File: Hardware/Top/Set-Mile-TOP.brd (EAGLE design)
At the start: 38 x 38 mm, 19 parts, among them U2 NRF52832_MODULE_MDBT42

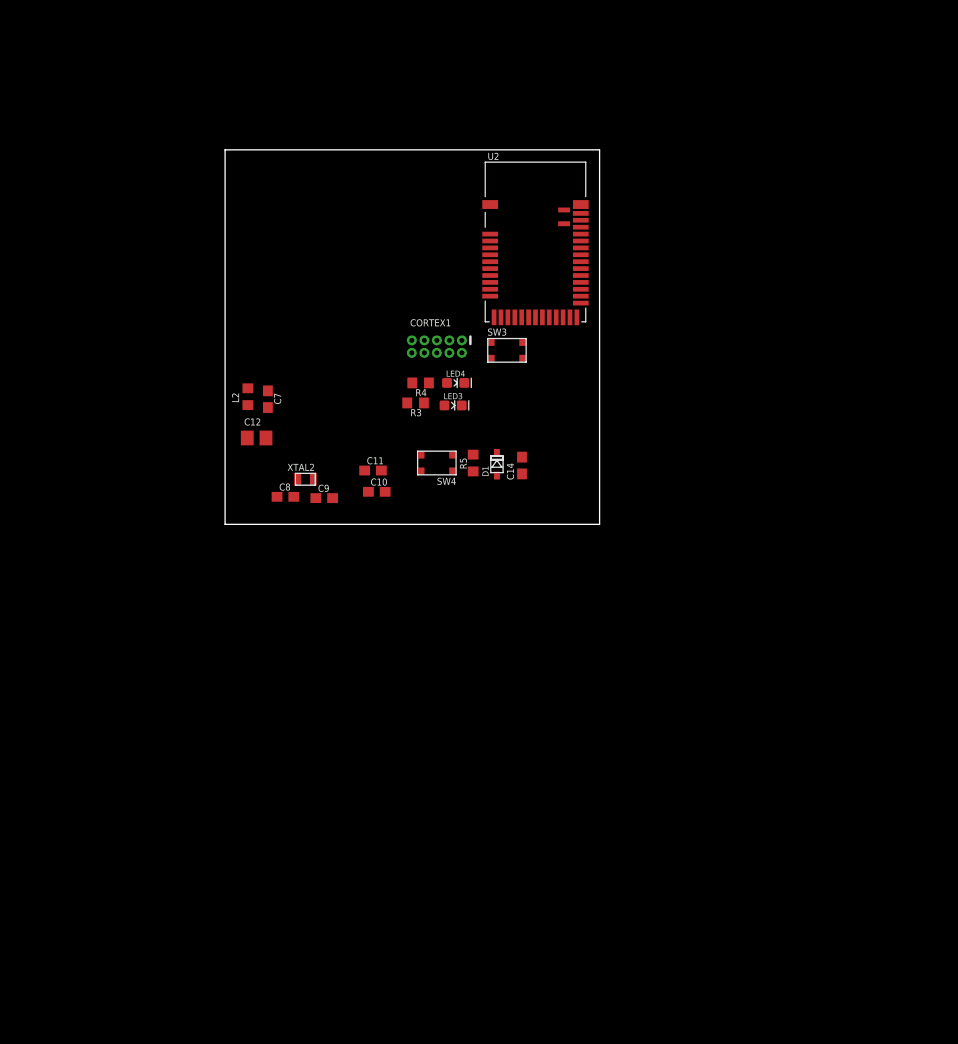
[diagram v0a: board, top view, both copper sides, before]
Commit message: Top Board Electronics Placed
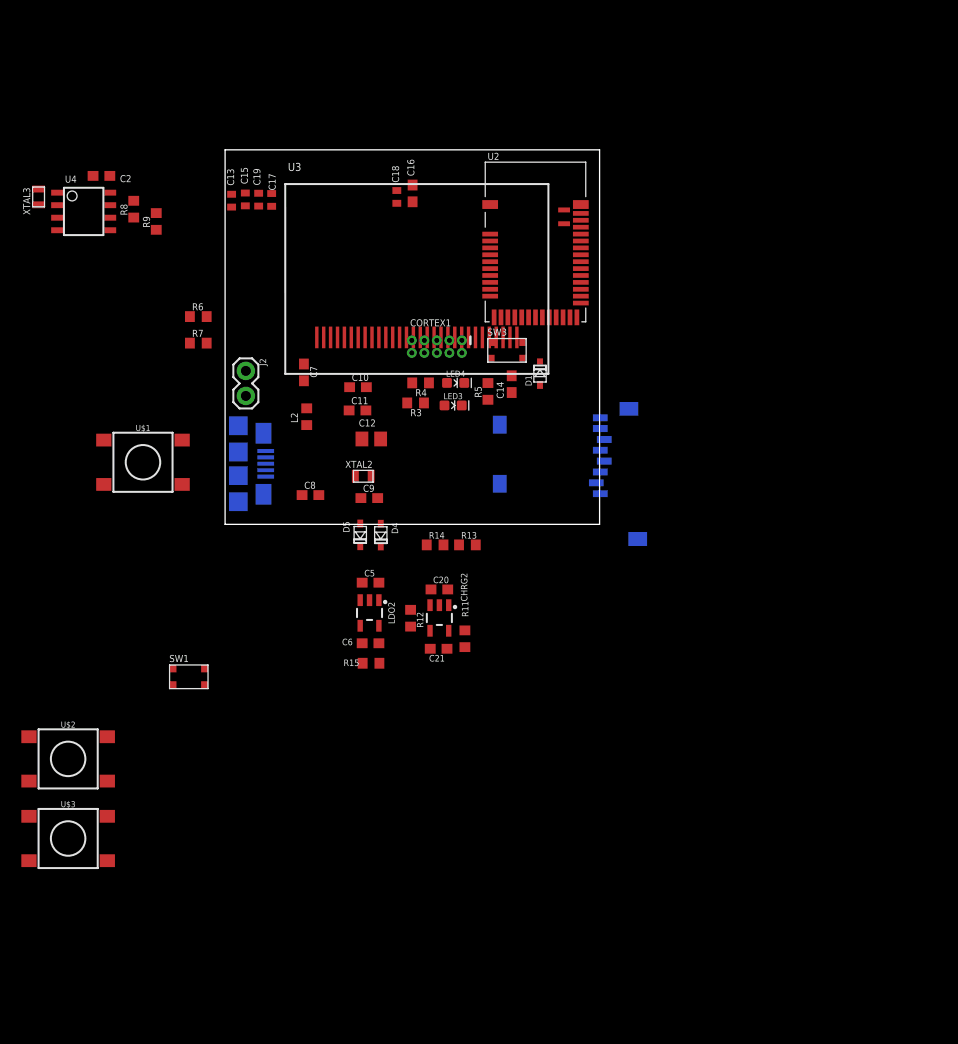
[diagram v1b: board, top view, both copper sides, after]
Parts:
- removed SW4: (no value), LinnesLab-Switches:BUTTON-GULLWING
- added C13, C15, C17, C18, C19: 2.2uF, LinnesLab-Passives:C0402
- added C16: 10uF, LinnesLab-Passives:C0603
- added C2, C5, C6: 1u, LinnesLab-Passives:C0603
- added C20, C21: 4.7u, LinnesLab-Passives:C0603
- added CHRG2: MCP73831, LinnesLab-Power:SOT23-5
- added D4, D5: (no value), LinnesLab-DiscreteSemi:USC
- added J2: (no value), LinnesLab-Connectors:1X02
- added LDO2: MIC5504, LinnesLab-Power:SOT23-5
- added R11: (no value), LinnesLab-Passives:R0603
- added R12, R13, R14, R15: 100k, LinnesLab-Passives:R0603
- added R6, R8, R9: 10k, LinnesLab-Passives:R0603
- added R7: 390k, LinnesLab-Passives:R0603
- added SD2: (no value), LinnesLab-Connectors:MICROSD
- added SW1: (no value), LinnesLab-Switches:BUTTON-GULLWING
- added U$1, U$2, U$3: SWITCH.MOM, LinnesLab-Switches:TACTILE_SWITCH_SMD_6.2MM_TALL
- added U3: (no value), LinnesLab-Displays:UG-2864HSWEG01_0.96IN_NO-WRAPAROUND
- added U4: PCF8523, LinnesLab-Clocks:SO8
- added USB2: USB.MICRO-BIGGERPADS, LinnesLab-Connectors:USB-MICRO-01.BIGGERPADS
- added XTAL3: 32.7680kHz, LinnesLab-Clocks:2-SMD.NOLEAD.2.0MMTO1.2MM
- moved C12 11.6 mm to (14.8, 8.66)
- moved C10 10.8 mm to (13.5, 13.9)
- moved D1 10.2 mm to (32.0, 15.3)
- moved C14 8.32 mm to (29.1, 14.2)
- moved R5 7.42 mm to (26.7, 13.5)
- moved L2 6.31 mm to (8.28, 10.9)
- moved C11 6.30 mm to (13.4, 11.6)
- moved XTAL2 5.88 mm to (14.0, 4.88)
- moved C9 4.57 mm to (14.6, 2.67)
- moved C7 4.56 mm to (8.00, 15.4)
- moved C8 2.55 mm to (8.66, 2.97)
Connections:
- new net BATT: R13.1, R14.2
- new net CD1: SD2.CD1
- new net CD2: SD2.CD2
- new net CHRG.STAT: CHRG2.1, R12.1
- new net CS.OLED: U3.13
- new net DC.OLED: U3.15
- new net N$1: R6.2, U3.11
- new net N$13: C16.2, U3.28
- new net N$15: C18.2, U3.27
- new net N$17: CHRG2.5, R11.2
- new net N$19: U4.2, XTAL3.P$1
- new net N$2: R7.1, U3.26
- new net N$20: U4.1, XTAL3.P$2
- new net N$3: C13.2, U3.2
- new net N$5: C13.1, U3.3
- new net N$7: C15.2, U3.4
- new net N$8: C15.1, U3.5
- new net RESET.OLED: U3.14
- new net SD.CS: SD2.2
- new net SW1: U$1.A1, U$2.A1, U$3.A1
- new net USB+: USB2.3
- new net USB-: USB2.2
- new net VBATT: U4.3
- new net VIN: C21.2, C5.2, CHRG2.4, D4.-, D5.-, LDO2.1, LDO2.3, R12.2
- new net VLIPO: C20.1, CHRG2.3, D4.+, J2.2, R13.2
- new net V_USB: D5.+, USB2.1
- net 3.3V: now also C17.2, C19.2, C2.1, C6.1, LDO2.5, R15.2, R8.2, R9.2, SD2.4, U3.6, U3.9, U4.8
- net DFU: now also SW1.3
- net GND: now also C16.1, C17.1, C18.1, C19.1, C2.2, C20.2, C21.1, C5.1, C6.2, CHRG2.2, J2.1, LDO2.2, R11.1, R14.1, R15.1, R6.1, R7.2, SD2.6, SD2.MT1, SD2.MT2, SW1.1, U$1.B1, U$1.B2, U$2.B1, U$2.B2, U$3.B1, U$3.B2, U3.1, U3.10, U3.12, U3.29, U3.30, U3.8, U4.4, USB2.5, USB2.S1, USB2.S2, USB2.S3, USB2.S4, USB2.S5, USB2.S6; no longer SW4.3
- net MISO: now also SD2.7
- net MOSI: now also SD2.3, U3.19
- net RESET: no longer SW4.1
- net SCK: now also SD2.5, U3.18
- net SCL: now also R8.1, U4.6
- net SDA: now also R9.1, U4.5

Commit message: updated board design to section 2
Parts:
- removed U$1, U$2, U$3: SWITCH.MOM, LinnesLab-Switches:TACTILE_SWITCH_SMD_6.2MM_TALL
- added C22: 100n, LinnesLab-Passives:C0603
- added C23, C24: 47p, LinnesLab-Passives:C0603
- added J1: (no value), LinnesLab-Connectors:1X07
- added JP2: (no value), LinnesLab-Switches:SMT-JUMPER_2_NO_SILK
- added LED5: RED, LinnesLab-LED:LED-0603
- added LED6: YELLOW, LinnesLab-LED:LED-0603
- added R1, R2: 0, LinnesLab-Passives:R0603
- added R17, R18: 27, LinnesLab-Passives:R0603
- added R19, R20: 1k, LinnesLab-Passives:R0603
- added SWITCH1, SWITCH2: SWITCH.MOM, LinnesLab-Switches:TACTILE_SWITCH_SMD_6.2MM_TALL
- added U5: FT231XS, LinnesLab-DigitalIC:SSOP20_L
- moved R9 81.8 mm to (-19.3, -50.2), turned to 0 degrees
- moved R8 79.3 mm to (-19.3, -46.7), turned to 0 degrees
- moved CORTEX1 33.8 mm to (55.1, 14.3)
- moved C15 10.4 mm to (9.40, 25.6)
- moved C13 10.4 mm to (8.15, 25.6)
- moved C19 10.3 mm to (10.6, 25.6)
- moved C17 10.2 mm to (11.8, 25.6)
- moved U2 0.42 mm to (31.4, 29.1)
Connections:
- net VBATT renamed VBAT
- removed net BATT: R13.1, R14.2
- removed net CD1: SD2.CD1
- removed net CHRG.STAT: CHRG2.1, R12.1
- removed net CS.OLED: U3.13
- removed net DC.OLED: U3.15
- removed net RESET.OLED: U3.14
- removed net RXD: U2.21
- removed net SD.CS: SD2.2
- removed net SW1: U$1.A1, U$2.A1, U$3.A1
- removed net TXD: U2.19
- new net !CTS: JP2.2, U5.9
- new net !DTR: U5.1
- new net A4/BATT: R13.1, R14.2, U2.5
- new net A6/TIA: J1.5, U2.7
- new net A7/PPG: J1.7, U2.8
- new net D11/SW1: SWITCH1.A1, U2.25
- new net D15/SW2: SWITCH2.A1, U2.29
- new net D16/CS.OLED: U2.30, U3.13
- new net D27/CHRG.STATUS: CHRG2.1, R12.1, U2.4
- new net D29/LED.CTRL: J1.6
- new net D3/RESET.OLED: U2.16, U3.14
- new net D4/DC.OLED: U2.15, U2.17, U3.15
- new net D5/CD1: SD2.CD1, U2.18
- new net D7/SD.CS: SD2.2, U2.20
- new net D9/LED.CTRL: U2.6
- new net FT3V3: U5.13
- new net N$23: R17.2, U5.12
- new net N$24: R18.2, U5.11
- new net N$25: LED5.C, R19.2
- new net N$26: LED6.C, R20.2
- new net RXD.FT: R2.1, U5.4
- new net RXD.NRF: R1.2, U2.21
- new net RXLED: R19.1, U5.17
- new net TXD.FT: R1.1, U5.20
- new net TXD.NRF: R2.2, U2.19
- new net TXLED: R20.1, U5.10
- net 3.3V: now also C22.2, LED5.A, LED6.A, U5.14, U5.3
- net GND: now also C22.1, C23.2, C24.1, JP2.1, SWITCH1.B1, SWITCH1.B2, SWITCH2.B1, SWITCH2.B2, U5.16, U5.6; no longer U$1.B1, U$1.B2, U$2.B1, U$2.B2, U$3.B1, U$3.B2
- net SCL: now also R9.1; no longer R8.1
- net SDA: now also R8.1; no longer R9.1
- net USB+: now also C23.1, R18.1
- net USB-: now also C24.2, R17.1
- net V_USB: now also U5.15

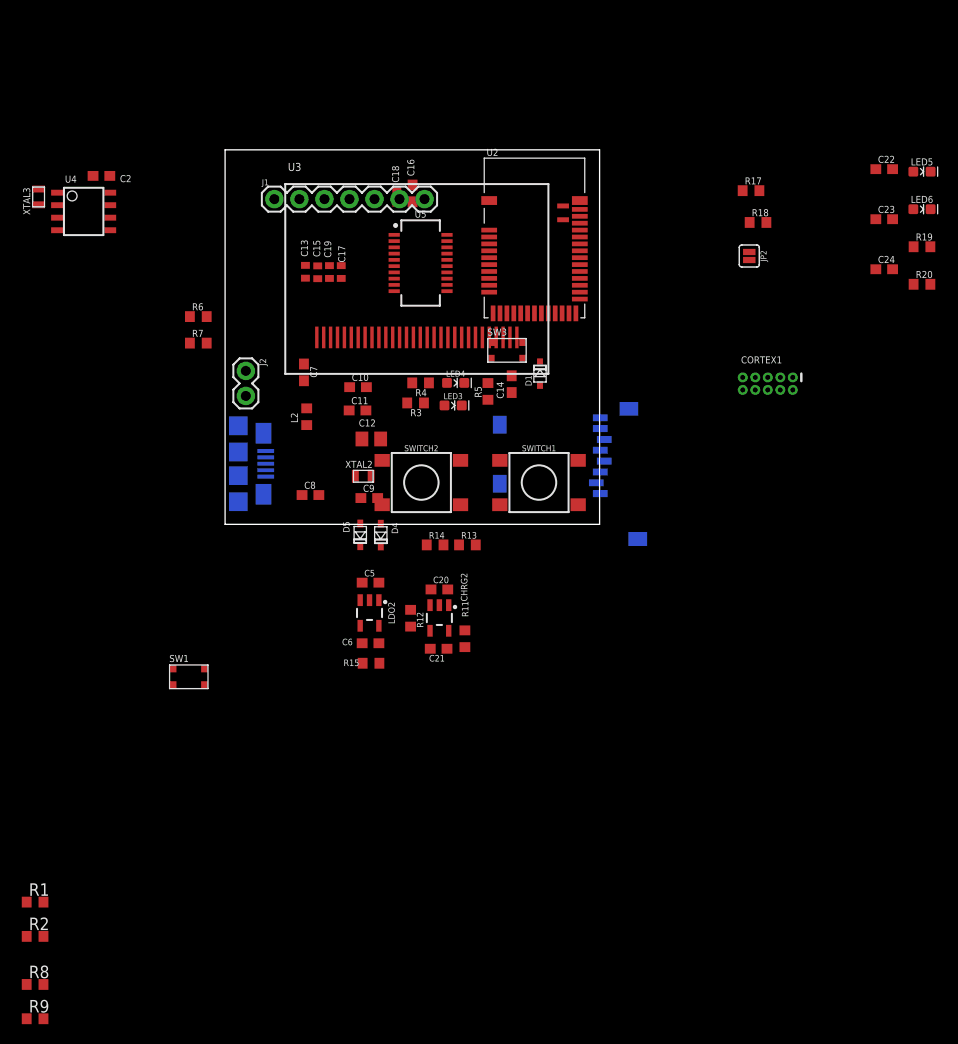
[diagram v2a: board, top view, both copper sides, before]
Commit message: routing bottom board and oranized top board
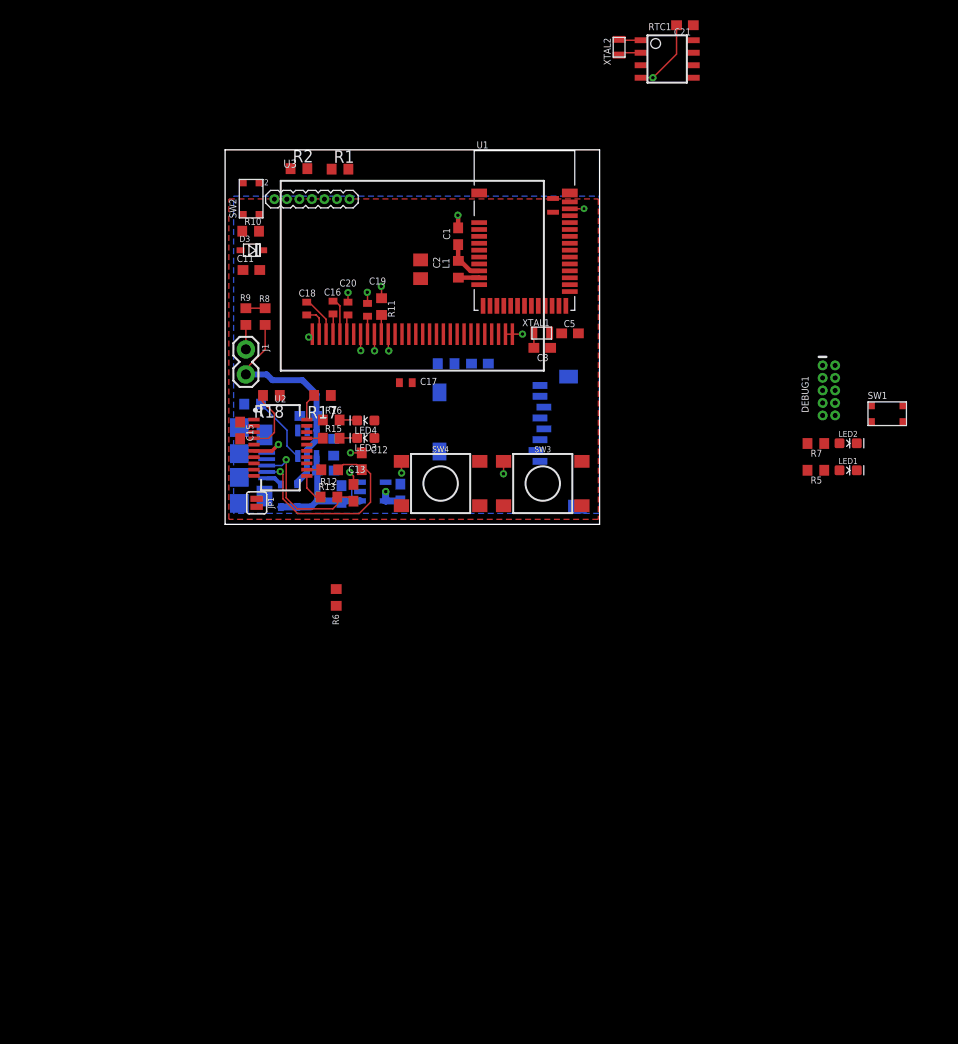
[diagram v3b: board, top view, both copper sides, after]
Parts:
- removed C22: 100n, LinnesLab-Passives:C0603
- removed C23, C24: 47p, LinnesLab-Passives:C0603
- removed C7: 1u, LinnesLab-Passives:C0603
- removed C8: (no value), LinnesLab-Passives:C0603
- removed CHRG2: MCP73831, LinnesLab-Power:SOT23-5
- removed CORTEX1: CORTEX_DEBUG_PTH, LinnesLab-Connectors:2X5-PTH-1.27MM
- removed D4, D5: (no value), LinnesLab-DiscreteSemi:USC
- removed JP2: (no value), LinnesLab-Switches:SMT-JUMPER_2_NO_SILK
- removed L2: 10u, LinnesLab-Passives:L0603
- removed LDO2: MIC5504, LinnesLab-Power:SOT23-5
- removed LED5: RED, LinnesLab-LED:LED-0603
- removed LED6: YELLOW, LinnesLab-LED:LED-0603
- removed R19, R20: 1k, LinnesLab-Passives:R0603
- removed SD2: (no value), LinnesLab-Connectors:MICROSD
- removed SWITCH1, SWITCH2: SWITCH.MOM, LinnesLab-Switches:TACTILE_SWITCH_SMD_6.2MM_TALL
- removed U4: PCF8523, LinnesLab-Clocks:SO8
- removed U5: FT231XS, LinnesLab-DigitalIC:SSOP20_L
- removed USB2: USB.MICRO-BIGGERPADS, LinnesLab-Connectors:USB-MICRO-01.BIGGERPADS
- removed XTAL3: 32.7680kHz, LinnesLab-Clocks:2-SMD.NOLEAD.2.0MMTO1.2MM
- added C1: 1u, LinnesLab-Passives:C0603
- added C3: (no value), LinnesLab-Passives:C0603
- added C4: 4.7u, LinnesLab-Passives:C0603
- added CHRG1: MCP73831, LinnesLab-Power:SOT23-5
- added D2, D3: (no value), LinnesLab-DiscreteSemi:USC
- added DEBUG1: CORTEX_DEBUG_PTH, LinnesLab-Connectors:2X5-PTH-1.27MM
- added JP1: (no value), LinnesLab-Switches:SMT-JUMPER_2_NO_SILK
- added L1: 10u, LinnesLab-Passives:L0603
- added LDO1: MIC5504, LinnesLab-Power:SOT23-5
- added LED1: RED, LinnesLab-LED:LED-0603
- added LED2: BLUE, LinnesLab-LED:LED-0603
- added R10: 10k, LinnesLab-Passives:R0603
- added R16: 1k, LinnesLab-Passives:R0603
- added RTC1: PCF8523, LinnesLab-Clocks:SO8
- added SD1: (no value), LinnesLab-Connectors:MICROSD
- added SW2: (no value), LinnesLab-Switches:BUTTON-GULLWING
- added SW4: SWITCH.MOM, LinnesLab-Switches:TACTILE_SWITCH_SMD_6.2MM_TALL
- added U1: NRF52832_MODULE_MDBT42, LinnesLab-Microcontrollers:BLE_MODULE_RAYTAC_MDBT42
- added USB1: USB.MICRO-BIGGERPADS, LinnesLab-Connectors:USB-MICRO-01.BIGGERPADS
- added XTAL1: 32.768kHz, LinnesLab-Clocks:2-SMD.NOLEAD.2.0MMTO1.2MM
- C10: value 300p -> 4.7u
- C11: value 300p -> 100n
- C12: value 10u -> 47p; device LinnesLab-Passives:C0805 -> LinnesLab-Passives:C0603
- C13: value 2.2uF -> 47p; device LinnesLab-Passives:C0402 -> LinnesLab-Passives:C0603
- C14: value 100n -> 10uF
- C15: value 2.2uF -> 100n; device LinnesLab-Passives:C0402 -> LinnesLab-Passives:C0603
- C16: value 10uF -> 2.2uF; device LinnesLab-Passives:C0603 -> LinnesLab-Passives:C0402
- C2: value 1u -> 10u; device LinnesLab-Passives:C0603 -> LinnesLab-Passives:C0805
- C20: value 4.7u -> 2.2uF; device LinnesLab-Passives:C0603 -> LinnesLab-Passives:C0402
- C21: value 4.7u -> 1u
- C5: value 1u -> (none)
- C9: value (none) -> 1u
- J1: device LinnesLab-Connectors:1X07 -> LinnesLab-Connectors:1X02
- J2: device LinnesLab-Connectors:1X02 -> LinnesLab-Connectors:1X07_1.27MM
- LED4: value BLUE -> YELLOW
- R1, R2: value 0 -> 10k
- R11: value (none) -> 10k
- R12, R13: value 100k -> 27
- R14: value 100k -> 390k
- R15: value 100k -> 1k
- R17, R18: value 27 -> 0
- R3: value 1k -> 100k
- R4: value 1k -> (none)
- R5: value 10k -> 1k
- R6, R8, R9: value 10k -> 100k
- R7: value 390k -> 1k
- SW3: value (none) -> SWITCH.MOM; device LinnesLab-Switches:BUTTON-GULLWING -> LinnesLab-Switches:TACTILE_SWITCH_SMD_6.2MM_TALL
- U2: value NRF52832_MODULE_MDBT42 -> FT231XS; device LinnesLab-Microcontrollers:BLE_MODULE_RAYTAC_MDBT42 -> LinnesLab-DigitalIC:SSOP20_L
- XTAL2: value 32.768kHz -> 32.7680kHz
- moved R2 82.4 mm to (7.49, 36.1)
- moved R1 80.5 mm to (11.7, 36.0)
- moved SW1 75.7 mm to (67.2, 11.2)
- moved R9 74.4 mm to (2.11, 21.1), turned to 90 degrees
- moved R8 71.7 mm to (4.06, 21.1), turned to 270 degrees
- moved C21 68.0 mm to (46.7, 50.6)
- moved R7 63.5 mm to (59.9, 8.20), turned to 180 degrees
- moved R18 52.4 mm to (4.70, 13.1)
- moved XTAL2 50.7 mm to (40.0, 48.4), turned to 90 degrees
- moved R17 48.2 mm to (9.88, 13.1)
- moved R11 34.8 mm to (15.9, 22.1), turned to 270 degrees
- moved R5 34.2 mm to (59.9, 5.49), turned to 180 degrees
- moved C2 33.7 mm to (19.8, 25.9), turned to 270 degrees
- moved U2 33.4 mm to (5.61, 7.77), turned to 270 degrees
- moved C5 32.4 mm to (35.0, 19.4)
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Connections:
- removed net VBAT: U4.3
- net !CTS: now also JP1.2, U2.9; no longer JP2.2, U5.9
- net !DTR: now also U2.1; no longer U5.1
- net 3.3V: now also C15.2, C2.2, C20.2, C21.1, C9.1, D3.-, DEBUG1.1, J2.4, LDO1.5, LED3.A, LED4.A, R1.2, R10.2, R2.2, R6.2, RTC1.8, SD1.4, U1.11, U2.14, U2.3; no longer C12.2, C17.2, C2.1, C22.2, C6.1, CORTEX1.1, D1.-, LDO2.5, LED5.A, LED6.A, R15.2, R5.2, R8.2, R9.2, SD2.4, U2.11, U4.8, U5.14, U5.3
- net A4/BATT: now also R8.1, R9.2, U1.5; no longer R13.1, R14.2, U2.5
- net A6/TIA: now also J2.6, U1.7; no longer J1.5, U2.7
- net A7/PPG: now also J2.7, U1.8; no longer J1.7, U2.8
- net CD2: now also SD1.CD2; no longer SD2.CD2
- net D11/SW1: now also SW3.A1, U1.25; no longer SWITCH1.A1, U2.25
- net D15/SW2: now also SW4.A1, U1.29; no longer SWITCH2.A1, U2.29
- net D16/CS.OLED: now also U1.30; no longer U2.30
- net D27/CHRG.STATUS: now also CHRG1.1, R3.1, U1.4; no longer CHRG2.1, R12.1, U2.4
- net D29/LED.CTRL: now also J2.5; no longer J1.6
- net D3/RESET.OLED: now also U1.16; no longer U2.16
- net D4/DC.OLED: now also U1.15, U1.17; no longer U2.15, U2.17
- net D5/CD1: now also SD1.CD1, U1.18; no longer SD2.CD1, U2.18
- net D7/SD.CS: now also SD1.2, U1.20; no longer SD2.2, U2.20
- net D9/LED.CTRL: now also U1.6; no longer U2.6
- net DFU: now also SW2.3, U1.34; no longer SW3.3, U2.34
- net DTR: now also C11.1; no longer C14.1
- net FRST: now also U1.38; no longer U2.38
- net FT3V3: now also U2.13; no longer U5.13
- net GND: now also C1.2, C13.2, C14.1, C15.1, C2.1, C20.1, C21.2, C3.1, C4.1, C5.2, C6.1, CHRG1.2, DEBUG1.3, DEBUG1.5, DEBUG1.7, DEBUG1.9, J1.1, J2.3, JP1.1, LDO1.2, LED1.C, LED2.C, R14.2, R4.1, R9.1, RTC1.4, SD1.6, SD1.MT1, SD1.MT2, SW2.1, SW3.B1, SW3.B2, SW4.B1, SW4.B2, U1.1, U1.12, U1.24, U1.39, U2.16, U2.6, USB1.5, USB1.S1, USB1.S2, USB1.S3, USB1.S4, USB1.S5, USB1.S6; no longer C11.2, C16.1, C18.1, C2.2, C20.2, C21.1, C22.1, C23.2, C24.1, C5.1, C6.2, C7.2, C8.1, CHRG2.2, CORTEX1.3, CORTEX1.5, CORTEX1.7, CORTEX1.9, J2.1, JP2.1, LDO2.2, LED3.C, LED4.C, R14.1, R15.1, R7.2, SD2.6, SD2.MT1, SD2.MT2, SW3.1, SWITCH1.B1, SWITCH1.B2, SWITCH2.B1, SWITCH2.B2, U2.1, U2.12, U2.24, U2.39, U4.4, U5.16, U5.6, USB2.5, USB2.S1, USB2.S2, USB2.S3, USB2.S4, USB2.S5, USB2.S6
- net LED1: now also R5.2, U1.31; no longer R3.2, U2.31
- net LED2: now also R7.2, U1.33; no longer R4.2, U2.33
- net MISO: now also SD1.7, U1.28; no longer SD2.7, U2.28
- net MOSI: now also SD1.3, U1.27; no longer SD2.3, U2.27
- net N$1: now also R11.2; no longer R6.2
- net N$10: now also LED2.A, R7.1; no longer LED4.A, R4.1
- net N$11: now also L1.1, U1.10; no longer L2.1, U2.10
- net N$12: now also C1.1, L1.2, U1.9; no longer C7.1, L2.2, U2.9
- net N$13: now also C14.2; no longer C16.2
- net N$14: now also DEBUG1.8; no longer CORTEX1.8
- net N$15: now also C17.2; no longer C18.2
- net N$17: now also CHRG1.5, R4.2; no longer CHRG2.5, R11.2
- net N$19: now also RTC1.2, XTAL2.P$1; no longer U4.2, XTAL3.P$1
- net N$2: now also R14.1; no longer R7.1
- net N$20: now also RTC1.1, XTAL2.P$2; no longer U4.1, XTAL3.P$2
- net N$23: now also R12.2, U2.12; no longer R17.2, U5.12
- net N$24: now also R13.2, U2.11; no longer R18.2, U5.11
- net N$25: now also LED3.C, R15.2; no longer LED5.C, R19.2
- net N$26: now also LED4.C, R16.2; no longer LED6.C, R20.2
- net N$3: now also C18.2; no longer C13.2
- net N$4: now also C3.2, U1.13, XTAL1.P$1; no longer C8.2, U2.13, XTAL2.P$1
- net N$5: now also C18.1; no longer C13.1
- net N$6: now also C5.1, U1.14, XTAL1.P$2; no longer C9.1, U2.14, XTAL2.P$2
- net N$7: now also C16.2; no longer C15.2
- net N$8: now also C16.1; no longer C15.1
- net N$9: now also LED1.A, R5.1; no longer LED3.A, R3.1
- net P0.09/NFC1: now also U1.22; no longer C11.1, U2.22
- net P0.10/NFC2: now also U1.23; no longer C10.1, U2.23
- net RESET: now also C11.2, D3.+, DEBUG1.10, R10.1, U1.35; no longer C14.2, CORTEX1.10, D1.+, R5.1, U2.35
- net RXD.FT: now also R18.1, U2.4; no longer R2.1, U5.4
- net RXD.NRF: now also R17.2, U1.21; no longer R1.2, U2.21
- net RXLED: now also R15.1, U2.17; no longer R19.1, U5.17
- net SCK: now also SD1.5, U1.26; no longer SD2.5, U2.26
- net SCL: now also J2.2, R2.1, RTC1.6, U1.3; no longer R9.1, U2.3, U4.6
- net SDA: now also J2.1, R1.1, RTC1.5, U1.2; no longer R8.1, U2.2, U4.5
- net SWCLK: now also DEBUG1.4, U1.36; no longer CORTEX1.4, U2.36
- net SWDIO: now also DEBUG1.2, U1.37; no longer CORTEX1.2, U2.37
- net SWO: now also DEBUG1.6, U1.32; no longer CORTEX1.6, U2.32
- net TXD.FT: now also R17.1, U2.20; no longer R1.1, U5.20
- net TXD.NRF: now also R18.2, U1.19; no longer R2.2, U2.19
- net TXLED: now also R16.1, U2.10; no longer R20.1, U5.10
- net USB+: now also C13.1, R13.1, USB1.3; no longer C23.1, R18.1, USB2.3
- net USB-: now also C12.2, R12.1, USB1.2; no longer C24.2, R17.1, USB2.2
- net VIN: now also C4.2, C6.2, CHRG1.4, D1.-, D2.-, LDO1.1, LDO1.3, R3.2; no longer C21.2, C5.2, CHRG2.4, D4.-, D5.-, LDO2.1, LDO2.3, R12.2
- net VLIPO: now also C10.1, CHRG1.3, D1.+, J1.2, R8.2; no longer C20.1, CHRG2.3, D4.+, J2.2, R13.2
- net V_USB: now also D2.+, U2.15, USB1.1; no longer D5.+, U5.15, USB2.1
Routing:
- net GND: track 0.00 -> 29.8 mm, vias 0 -> 15
- net VLIPO: track 0.00 -> 23.8 mm
- net USB-: track 0.00 -> 21.0 mm, vias 0 -> 1
- net VIN: track 0.00 -> 15.5 mm
- net USB+: track 0.00 -> 14.6 mm, vias 0 -> 1
- net N$17: track 0.00 -> 6.86 mm
- net RXD.FT: track 0.00 -> 6.62 mm
- net 3.3V: track 0.00 -> 6.28 mm, vias 0 -> 1
- net N$5: track 0.00 -> 4.20 mm
- net N$12: track 0.00 -> 4.19 mm
- net N$8: track 0.00 -> 3.80 mm
- net N$3: track 0.00 -> 3.03 mm
- net N$24: track 0.00 -> 3.00 mm
- net TXD.FT: track 0.00 -> 2.76 mm
- net N$19: track 0.00 -> 2.33 mm
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- added copper zone on layer 1, net 3.3V
- added copper zone on layer 16, net GND
